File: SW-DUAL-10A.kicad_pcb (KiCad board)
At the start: 2 copper layers, 100 x 74 mm, 26 parts, among them J1 SW1, J2 SW2, J3 GND +SW1, J4 GND +SW2, J5 GND +12V, U1 BTS7002-1EPP, U2 BTS7002-1EPP

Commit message: everything is on the layout, needs a lot of tuning
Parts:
- J3: value GND +SW1 -> Screw_Terminal_01x02; footprint SamacSys_Parts:VP0265840000G -> TerminalBlock_Phoenix:TerminalBlock_Phoenix_MKDS-1,5-2-5.08_1x02_P5.08mm_Horizontal
- J4: value GND +SW2 -> Screw_Terminal_01x02; footprint SamacSys_Parts:VP0265840000G -> TerminalBlock_Phoenix:TerminalBlock_Phoenix_MKDS-1,5-2-5.08_1x02_P5.08mm_Horizontal
- J5: value GND +12V -> PWRIN
- R11, R12: footprint Resistor_SMD:R_0603_1608Metric_Pad0.98x0.95mm_HandSolder -> Resistor_THT:R_Axial_DIN0207_L6.3mm_D2.5mm_P7.62mm_Horizontal
- RGND1: renamed from R1; footprint Resistor_SMD:R_0805_2012Metric_Pad1.20x1.40mm_HandSolder -> Resistor_SMD:R_0603_1608Metric_Pad0.98x0.95mm_HandSolder
- RGND2: renamed from R2; footprint Resistor_SMD:R_0805_2012Metric_Pad1.20x1.40mm_HandSolder -> Resistor_SMD:R_0603_1608Metric_Pad0.98x0.95mm_HandSolder
- moved RPD1 64.7 mm to (114.0, 81.5), turned to -90 degrees
- moved R11 63.7 mm to (115.2, 99.6), turned to -90 degrees
- moved R12 60.3 mm to (118.8, 107.2), turned to 90 degrees
- moved COUT1 59.7 mm to (115.6, 81.5), turned to 90 degrees
- moved COUT2 57.0 mm to (115.2, 128.0), turned to 90 degrees
- moved RPD2 56.8 mm to (113.5, 128.0), turned to -90 degrees
- moved CVS1 56.0 mm to (120.6, 82.5)
- moved CVS2 51.7 mm to (120.4, 129.0)
- moved D1 50.0 mm to (124.6, 102.3), turned to 90 degrees
- moved R9 47.7 mm to (126.7, 82.3), turned to 180 degrees
- moved R6 34.8 mm to (127.3, 133.9), turned to 180 degrees
- moved R7 32.4 mm to (127.3, 132.2), turned to 180 degrees
- moved R8 30.4 mm to (127.3, 130.4), turned to 180 degrees
- moved R10 28.4 mm to (127.3, 128.7), turned to 180 degrees
- moved U1 11.1 mm to (118.4, 86.2)
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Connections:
- J3 pad 1: /SW1OUT -> GND
- J4 pad 1: /SW2OUT -> GND

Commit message: updates
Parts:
- U1: footprint Package_SO:Infineon_PG-TSDSO-14-22 -> SamacSys_Parts:SOP65P600X115-15N
- moved J1 4.71 mm to (149.0, 77.6)
- moved R9 1.81 mm to (125.3, 83.5)
- moved R5 1.66 mm to (125.3, 85.0)
- moved R4 1.54 mm to (125.3, 86.5)
- moved R3 1.46 mm to (125.3, 88.0)
- moved U1 0.10 mm to (118.4, 86.3)
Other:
- board size 100 x 74 mm -> 74.2 x 67 mm

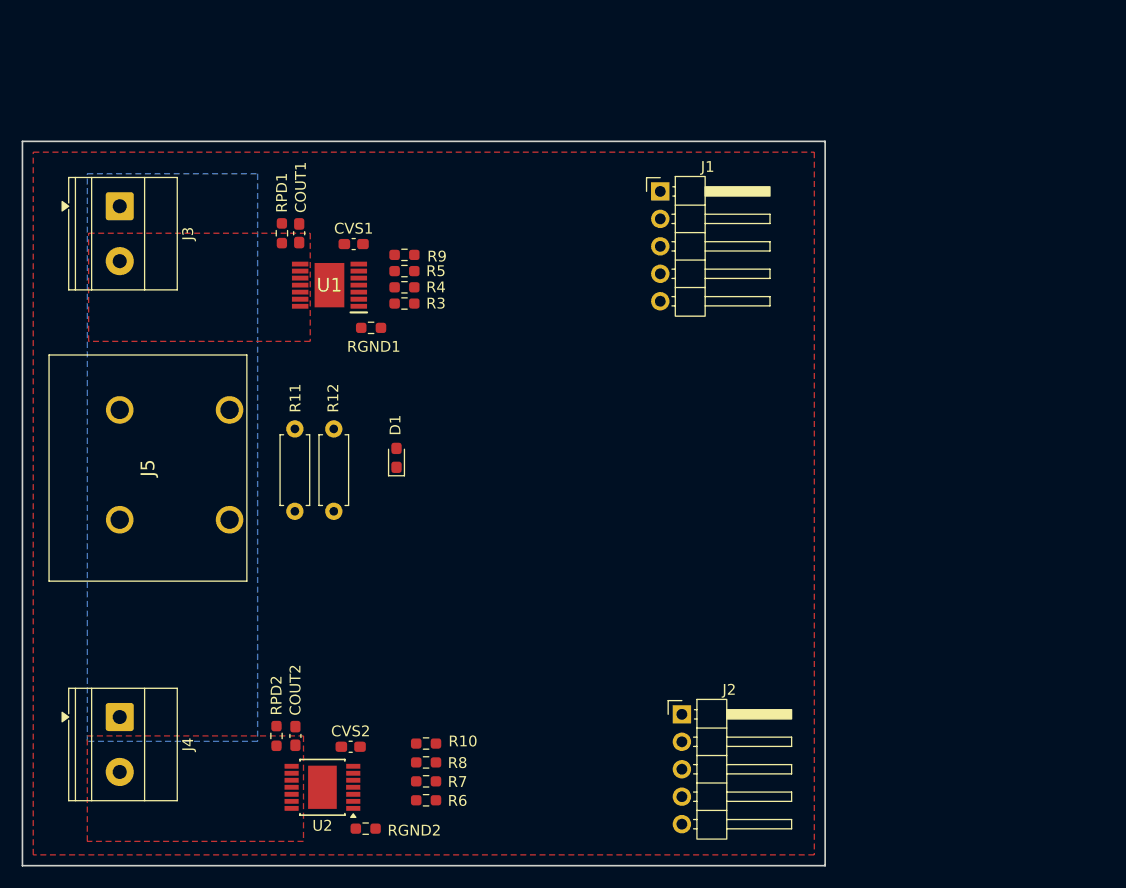
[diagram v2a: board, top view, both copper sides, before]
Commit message: added some mounting holes, pretty much finished, send it to the fab
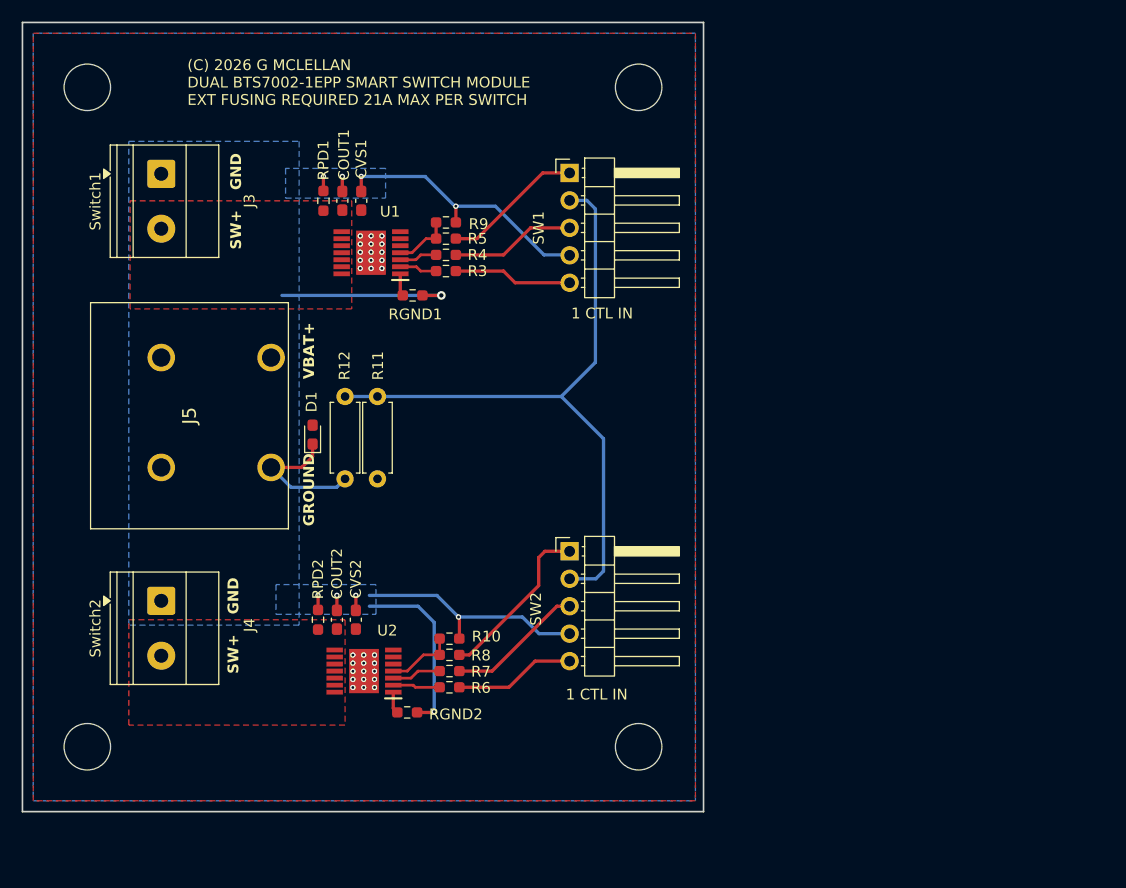
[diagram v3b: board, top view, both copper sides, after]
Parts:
- added H1: M4 4.3mm, MountingHole:MountingHole_4.3mm_M4, F.Cu at (96.0, 68.0)
- added H2: M4 4.3mm, MountingHole:MountingHole_4.3mm_M4, F.Cu at (96.0, 129.0)
- added H3: M4 4.3mm, MountingHole:MountingHole_4.3mm_M4, F.Cu at (147.0, 68.0)
- added H4: M4 4.3mm, MountingHole:MountingHole_4.3mm_M4, F.Cu at (147.0, 129.0)
- J3: value Screw_Terminal_01x02 -> Switch1
- J4: value Screw_Terminal_01x02 -> Switch2
- U2: footprint Package_SO:Infineon_PG-TSDSO-14-22 -> SamacSys_Parts:SOP65P600X115-15N
- moved J2 18.3 mm to (140.6, 110.9)
- moved CVS2 11.8 mm to (120.8, 117.2), turned to 90 degrees
- moved COUT2 11.4 mm to (119.1, 117.2)
- moved J4 11.4 mm to (102.8, 115.5)
- moved RPD2 11.4 mm to (117.3, 117.2)
- moved U2 11.4 mm to (121.6, 122.0)
- moved RGND2 11.4 mm to (125.6, 125.8)
- moved R6 10.7 mm to (129.5, 123.5)
- moved R7 10.4 mm to (129.5, 122.0)
- moved R8 10.2 mm to (129.5, 120.5)
- moved R10 9.94 mm to (129.5, 119.0)
- moved J1 8.56 mm to (140.6, 75.9)
- moved R11 8.21 mm to (122.8, 96.6)
- moved D1 8.05 mm to (116.8, 100.1)
- moved J5 6.18 mm to (102.8, 93.0)
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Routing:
- net GND: track 0.00 -> 101.0 mm, vias 0 -> 10
- net /VS: track 0.00 -> 62.6 mm
- net /SW2IS: track 0.00 -> 15.8 mm
- net /SW1IS: track 0.00 -> 13.0 mm
- net /SW2DEN: track 0.00 -> 12.7 mm
- net /SW1DEN: track 0.00 -> 11.6 mm
- net /SW2IN: track 0.00 -> 11.3 mm
- net /SW1IN: track 0.00 -> 11.0 mm
- net /SW2IS_PD: track 0.00 -> 6.41 mm
- net /SW1IS_PD: track 0.00 -> 5.35 mm
- net Net-(U2-DEN): track 0.00 -> 4.56 mm
- net Net-(U2-IN): track 0.00 -> 4.47 mm
- net Net-(U1-DEN): track 0.00 -> 3.50 mm
- net Net-(U1-IN): track 0.00 -> 3.48 mm
- net Net-(U1-GND): track 0.00 -> 2.09 mm
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- added copper zone on B.Cu, net +12V
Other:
- board size 74.2 x 67 mm -> 63 x 73 mm
- board text added: "(C) 2026 G MCLELLAN DUAL BTS7002-1EPP SMART SWITCH MODULE EXT FUSING REQUIRED 21A MAX PER SWITCH"
- board text added: "1 CTL IN"
- board text added: "GND"
- board text added: "GROUND"
- board text added: "SW+"
- board text added: "VBAT+"
